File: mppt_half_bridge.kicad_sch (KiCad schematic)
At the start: 29 parts, among them Q1 IRLZ44N, Q2 IRLZ44N, U1 INA181

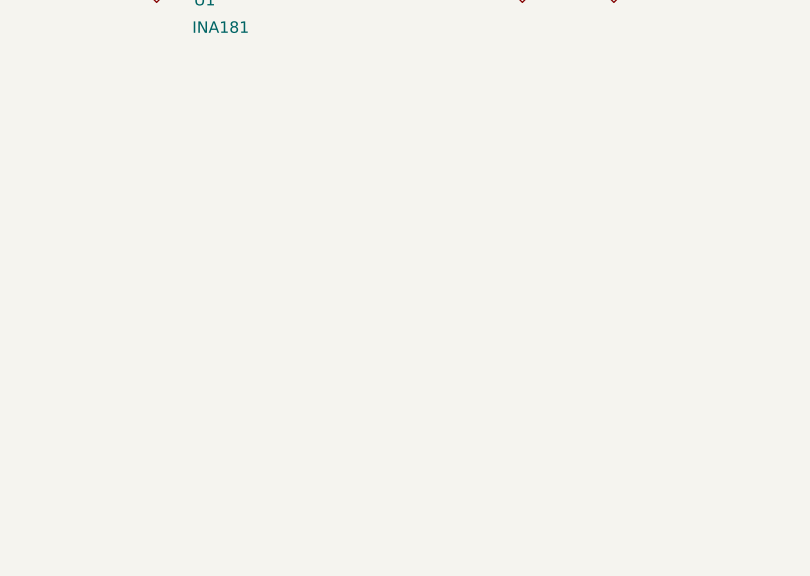
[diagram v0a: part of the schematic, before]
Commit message: Add 3.3V LDO
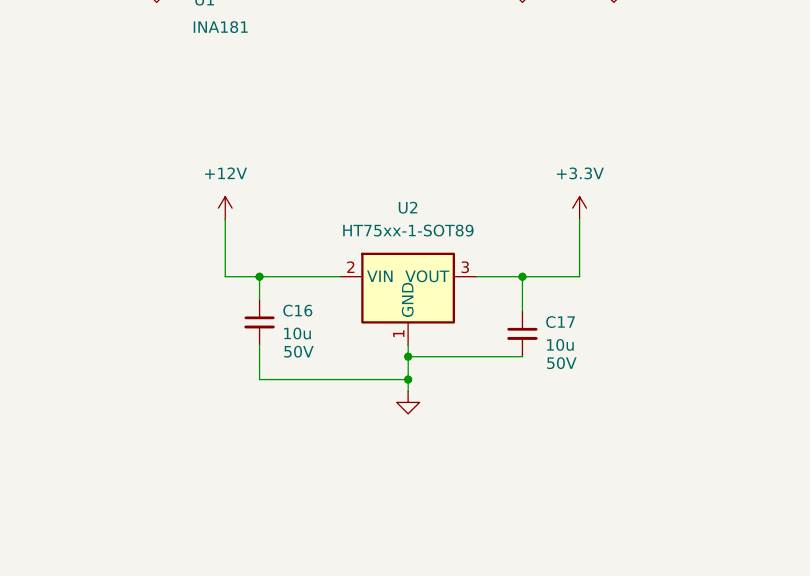
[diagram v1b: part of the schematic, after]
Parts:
- added C16, C17: 10u, symbol Device:C_Small
- added U2: HT75xx-1-SOT89, Package_TO_SOT_SMD:SOT-89-3, symbol Regulator_Linear:HT75xx-1-SOT89
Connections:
- net +12V: now also C16.1, U2.2 (VIN)
- net +3.3V: now also C17.1, U2.3 (VOUT)
- net GND: now also C16.2, C17.2, U2.1 (GND)

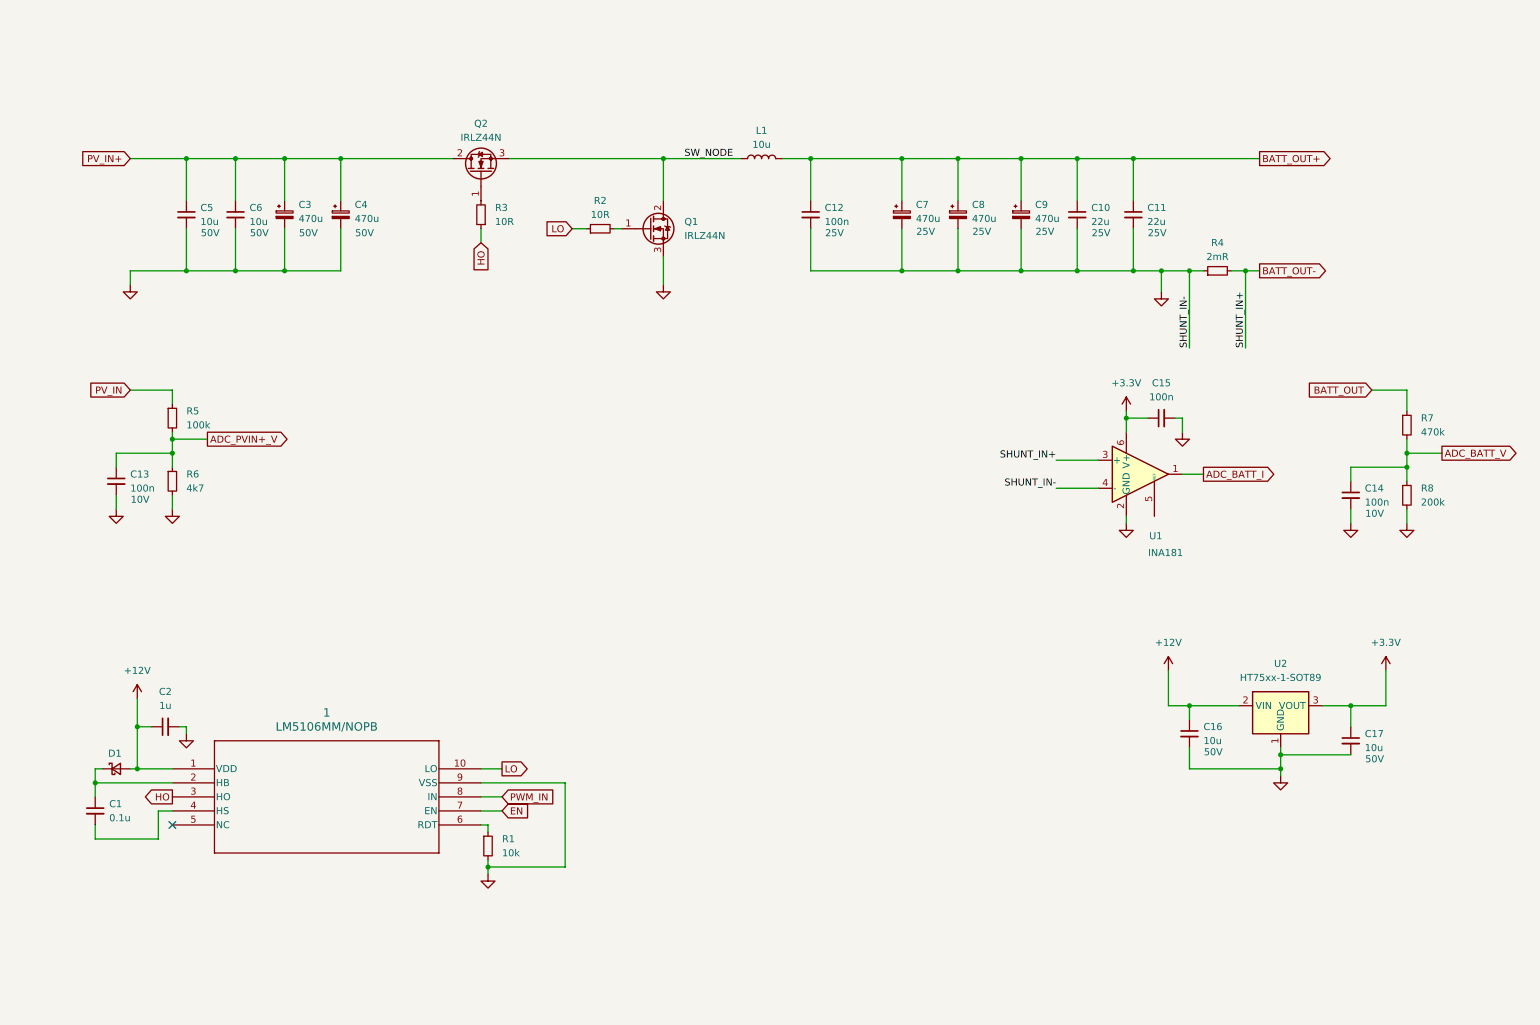
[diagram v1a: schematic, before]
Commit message: Add notes and generate pdf
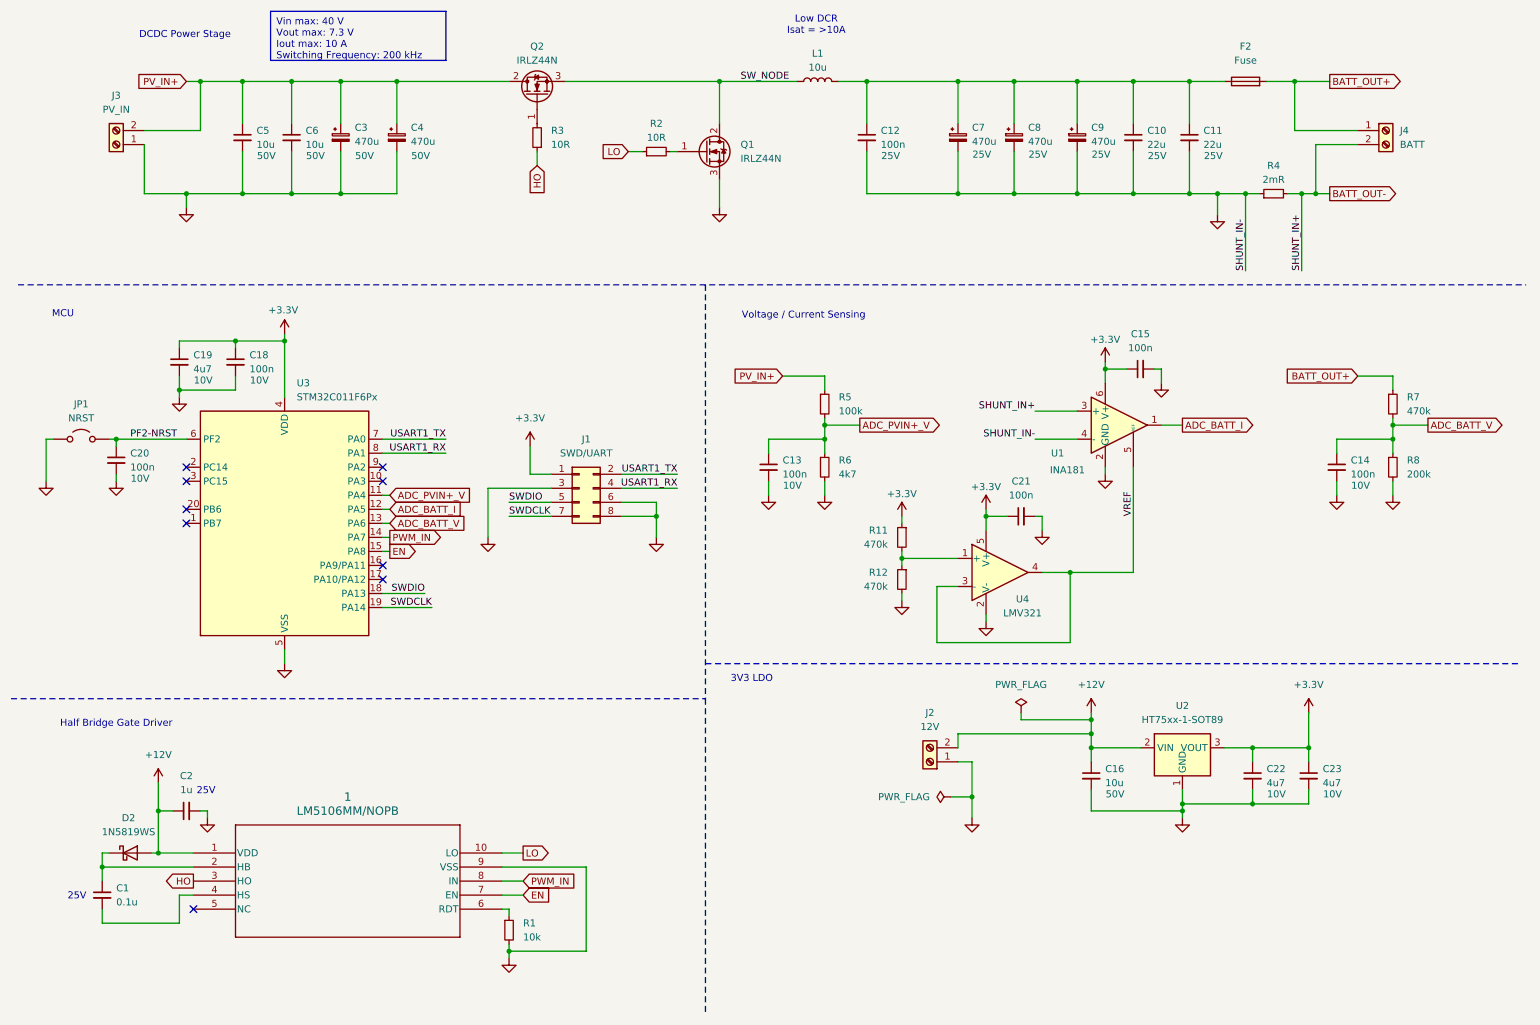
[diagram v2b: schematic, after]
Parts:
- removed C17: 10u, symbol Device:C_Small
- removed D1: D_Schottky_Small, symbol Device:D_Schottky_Small
- added C18, C20, C21: 100n, Capacitor_SMD:C_0603_1608Metric, symbol Device:C_Small
- added C19, C22, C23: 4u7, Capacitor_SMD:C_0603_1608Metric, symbol Device:C_Small
- added D2: 1N5819WS, Diode_SMD:D_SOD-323, symbol Diode:1N5819WS
- added F2: Fuse, Fuse:Fuse_1210_3225Metric, symbol Device:Fuse
- added J1: SWD/UART, Connector_PinHeader_2.54mm:PinHeader_2x05_P2.54mm_Vertical, symbol Connector_Generic:Conn_02x04_Odd_Even
- added J2: 12V, symbol Connector:Screw_Terminal_01x02
- added J3: PV_IN, symbol Connector:Screw_Terminal_01x02
- added J4: BATT, symbol Connector:Screw_Terminal_01x02
- added JP1: NRST, TestPoint:TestPoint_2Pads_Pitch2.54mm_Drill0.8mm, symbol Jumper:Jumper_2_Open
- added R11, R12: 470k, Resistor_SMD:R_0603_1608Metric, symbol Device:R_Small
- added U3: STM32C011F6Px, Package_SO:TSSOP-20_4.4x6.5mm_P0.65mm, symbol MCU_ST_STM32C0:STM32C011F6Px
- added U4: LMV321, Package_TO_SOT_SMD:SOT-23-5, symbol Amplifier_Operational:LMV321
- 1: footprint MUB10A -> footprints:MUB10A
- C1, C10, C11, C12, C13, C14, C15, C16, C2, C5, C6: footprint (none) -> Capacitor_SMD:C_0603_1608Metric
- C3, C4, C7, C8, C9: footprint (none) -> Capacitor_SMD:CP_Elec_4x5.4
- R1, R2, R3, R5, R6, R7, R8: footprint (none) -> Resistor_SMD:R_0603_1608Metric
- R4: footprint (none) -> Resistor_SMD:R_1210_3225Metric
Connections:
- net BATT_OUT is gone; now on net BATT_OUT+: R7.1
- net PV_IN is gone; now on net PV_IN+: R5.1
- net +12V: now also D2.2 (A), J2.2 (Pin_2)
- net +3.3V: now also C18.1, C19.1, C21.1, C22.1, C23.1, J1.1 (Pin_1), R11.1, U3.4 (VDD), U4.5 (V+)
- net ADC_BATT_I: now also U3.12 (PA5)
- net ADC_BATT_V: now also U3.13 (PA6)
- net ADC_PVIN+_V: now also U3.11 (PA4)
- net BATT_OUT+: now also F2.2, J4.1 (Pin_1); no longer C10.1, C11.1, C12.1, C7.1, C8.1, C9.1, L1.2
- net BATT_OUT-: now also J4.2 (Pin_2)
- net EN: now also U3.15 (PA8)
- net GND: now also C18.2, C19.2, C20.2, C21.2, C22.2, C23.2, J1.3 (Pin_3), J1.6 (Pin_6), J1.8 (Pin_8), J2.1 (Pin_1), J3.1 (Pin_1), JP1.1 (A), R12.2, U3.5 (VSS), U4.2 (V-)
- net PV_IN+: now also J3.2 (Pin_2)
- net PWM_IN: now also U3.14 (PA7)
- net at 1.2 (HB), C1.1: now also D2.1 (K)
- net VREF: now reaches U1.5 (REF)
- net VREF: now also U4.3 (-), U4.4
- new net: C10.1, C11.1, C12.1, C7.1, C8.1, C9.1, F2.1, L1.2
- new net: R11.2, R12.1, U4.1 (+)
- new net PF2-NRST: C20.1, JP1.2 (B), U3.6 (PF2)
- new net SWDCLK: J1.7 (Pin_7), U3.19 (PA14)
- new net SWDIO: J1.5 (Pin_5), U3.18 (PA13)
- new net USART1_RX: J1.4 (Pin_4), U3.8 (PA1)
- new net USART1_TX: J1.2 (Pin_2), U3.7 (PA0)
- no-connect marks 1 -> 9
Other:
- note added: "25V"
- note added: "3V3 LDO"
- note added: "DCDC Power Stage"
- note added: "Half Bridge Gate Driver"
- note added: "Low DCR Isat = >10A"
- note added: "MCU"
- note added: "Voltage / Current Sensing"
- title: (none) -> MPPT Charge Controller
- moved on the sheet: 1, C1, C10, C11, C12, C13, C14, C15, C16, C2, C3, C4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
